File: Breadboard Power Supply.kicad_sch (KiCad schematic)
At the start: 15 parts, among them J1 Conn_01x02, J2 Conn_01x02, J3 Conn_01x03, J4 Screw_Terminal_01x02, J5 Barrel_Jack, U1 LM7805_TO220, U2 LM317_TO-220

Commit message: footprints
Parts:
- C1, C2, C3: footprint (none) -> Capacitor_THT:C_Disc_D3.0mm_W1.6mm_P2.50mm
- D1: footprint (none) -> LED_THT:LED_D5.0mm
- J1, J2: footprint (none) -> Connector_PinHeader_2.54mm:PinHeader_1x02_P2.54mm_Vertical
- J3: footprint (none) -> Connector_PinHeader_2.54mm:PinHeader_1x03_P2.54mm_Vertical
- J4: footprint (none) -> TerminalBlock:TerminalBlock_bornier-2_P5.08mm
- J5: footprint (none) -> Connector_BarrelJack:BarrelJack_SwitchcraftConxall_RAPC10U_Horizontal
- R1, R2, R3: footprint (none) -> PCM_Resistor_THT_AKL:R_Axial_DIN0204_L3.6mm_D1.6mm_P7.62mm_Horizontal
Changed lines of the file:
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@@
 			)
 		)
-		(property "Footprint" ""
+		(property "Footprint" "Capacitor_THT:C_Disc_D3.0mm_W1.6mm_P2.50mm"
 			(at 87.3252 66.04 0)
 			(effects
@@
 			)
 		)
-		(property "Footprint" ""
+		(property "Footprint" "PCM_Resistor_THT_AKL:R_Axial_DIN0204_L3.6mm_D1.6mm_P7.62mm_Horizontal"
 			(at 66.04 55.118 90)
 			(effects
@@
 			)
 		)
-		(property "Footprint" ""
+		(property "Footprint" "LED_THT:LED_D5.0mm"
 			(at 66.04 40.64 0)
 			(effects
@@
 			)
 		)
-		(property "Footprint" ""
+		(property "Footprint" "Capacitor_THT:C_Disc_D3.0mm_W1.6mm_P2.50mm"
 			(at 67.0052 66.04 0)
 			(effects
@@
 			)
 		)
-		(property "Footprint" ""
+		(property "Footprint" "Connector_PinHeader_2.54mm:PinHeader_1x02_P2.54mm_Vertical"
 			(at 66.04 72.39 0)
 			(effects
@@
 			)
 		)
-		(property "Footprint" ""
+		(property "Footprint" "TerminalBlock:TerminalBlock_bornier-2_P5.08mm"
 			(at 90.17 82.55 0)
 			(effects
@@
 			)
 		)
-		(property "Footprint" ""
+		(property "Footprint" "PCM_Resistor_THT_AKL:R_Axial_DIN0204_L3.6mm_D1.6mm_P7.62mm_Horizontal"
 			(at 86.36 55.118 90)
 			(effects
@@
 			)
 		)
-		(property "Footprint" ""
+		(property "Footprint" "PCM_Resistor_THT_AKL:R_Axial_DIN0204_L3.6mm_D1.6mm_P7.62mm_Horizontal"
 			(at 76.2 55.118 90)
 			(effects
@@
 			)
 		)
-		(property "Footprint" ""
+		(property "Footprint" "Connector_BarrelJack:BarrelJack_SwitchcraftConxall_RAPC10U_Horizontal"
 			(at 67.31 26.416 0)
 			(effects
@@
 			)
 		)
-		(property "Footprint" ""
+		(property "Footprint" "Connector_PinHeader_2.54mm:PinHeader_1x02_P2.54mm_Vertical"
 			(at 86.36 72.39 0)
 			(effects
@@
 			)
 		)
-		(property "Footprint" ""
+		(property "Footprint" "Connector_PinHeader_2.54mm:PinHeader_1x03_P2.54mm_Vertical"
 			(at 67.31 83.82 0)
 			(effects
@@
 			)
 		)
-		(property "Footprint" ""
+		(property "Footprint" "Capacitor_THT:C_Disc_D3.0mm_W1.6mm_P2.50mm"
 			(at 77.1652 66.04 0)
 			(effects

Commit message: schematic + placing
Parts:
- removed J5: Barrel_Jack, Connector_BarrelJack:BarrelJack_SwitchcraftConxall_RAPC10U_Horizontal, symbol Connector:Barrel_Jack
- added J5: Barrel_Jack_Switch, Connector_BarrelJack:BarrelJack_Horizontal, symbol Connector:Barrel_Jack_Switch
- added J6: Conn_01x03, Connector_PinHeader_2.54mm:PinHeader_1x03_P2.54mm_Vertical, symbol Connector_Generic:Conn_01x03
- added J7: Screw_Terminal_01x02, TerminalBlock:TerminalBlock_bornier-2_P5.08mm, symbol Connector:Screw_Terminal_01x02
- D1: footprint LED_THT:LED_D5.0mm -> (none)
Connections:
- net 12V: now reaches S1.1
- net 12V: now also C1.1, R1.2, U1.1 (VI), U2.3 (VI)
- net PWR_input: now reaches S1.2
- net PWR_input: now also J5.1
- net 5V: now reaches C3.1
- net 5V: now also J3.1 (Pin_1), U1.3 (VO), J6.1 (Pin_1)
- net GND: now reaches C3.2
- net GND: now also C1.2, C2.2, D1.1 (K), J1.2 (Pin_2), J2.2 (Pin_2), J4.2 (Pin_2), R3.1, U1.2 (GND), J5.2, J5.3, J7.2 (Pin_2)
- net at R1.1: now also D1.2 (A)
- net PWR_output: now reaches J1.1 (Pin_1)
- net PWR_output: now also J2.1 (Pin_1), J3.2 (Pin_2), J4.1 (Pin_1), J6.2 (Pin_2), J7.1 (Pin_1)
- net at U2.1 (ADJ): now also R2.1, R3.2
- net 3.3V: now reaches U2.2 (VO)
- net 3.3V: now also C2.1, J3.3 (Pin_3), R2.2, J6.3 (Pin_3)
- no-connect marks 0 -> 1
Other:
- moved on the sheet: C1, C2, C3, J1, J3, J4, R1, R2, R3, S1, U1, U2

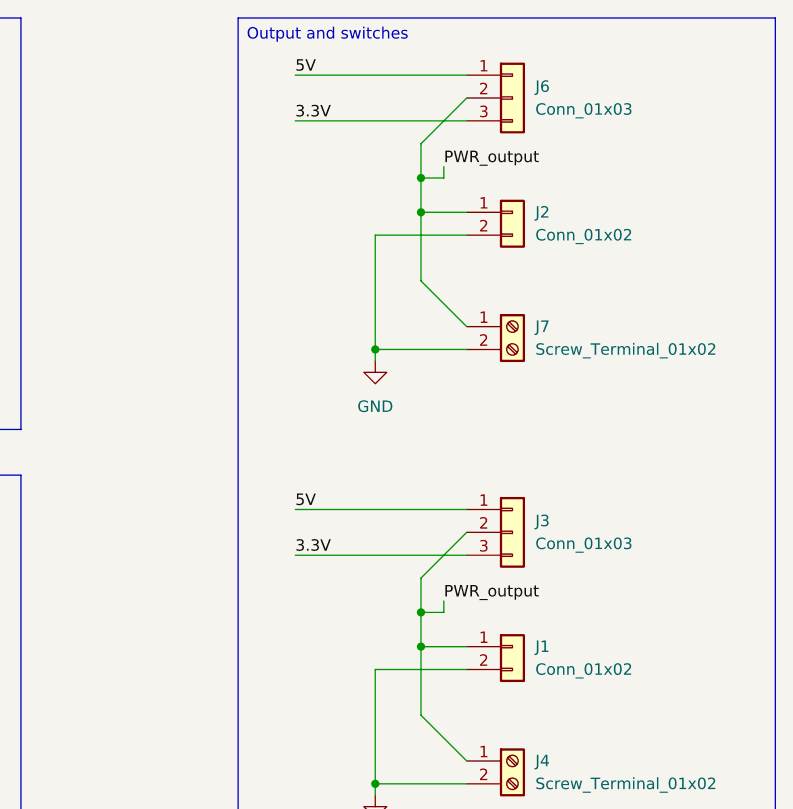
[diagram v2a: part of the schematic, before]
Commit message: fix short circuit pwr_output
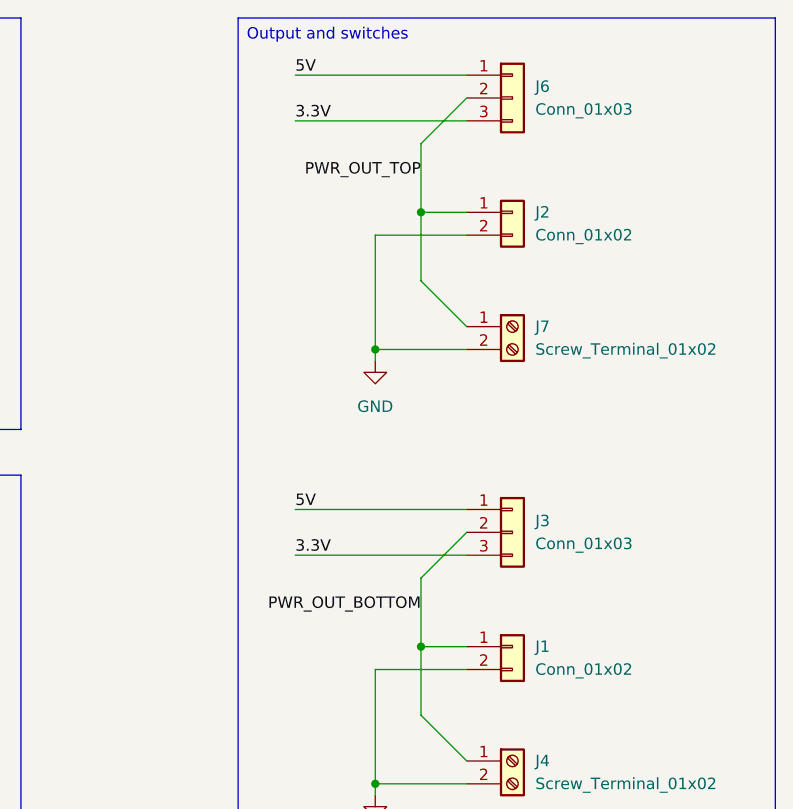
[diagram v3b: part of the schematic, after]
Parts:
- D1: footprint (none) -> PCM_LED_THT_AKL:LED_D5.0mm
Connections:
- net PWR_output renamed PWR_OUT_BOTTOM
- net PWR_OUT_BOTTOM: no longer J2.1 (Pin_1), J6.2 (Pin_2), J7.1 (Pin_1)
- new net PWR_OUT_TOP: J2.1 (Pin_1), J6.2 (Pin_2), J7.1 (Pin_1)
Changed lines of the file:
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@@
-	)
-	(junction
-		(at 209.55 63.5)
-		(diameter 0)
-		(color 0 0 0 0)
 	)
 	(junction
@@
 	(junction
 		(at 101.6 78.74)
-		(diameter 0)
-		(color 0 0 0 0)
-	)
-	(junction
-		(at 209.55 111.76)
 		(diameter 0)
 		(color 0 0 0 0)
@@
 	(wire
 		(pts
-			(xy 209.55 111.76) (xy 209.55 107.95)
-		)
-		(stroke
-			(width 0)
-			(type default)
-		)
-	)
-	(wire
-		(pts
 			(xy 204.47 118.11) (xy 214.63 118.11)
 		)
@@
 	(wire
 		(pts
-			(xy 209.55 63.5) (xy 209.55 59.69)
-		)
-		(stroke
-			(width 0)
-			(type default)
-		)
-	)
-	(wire
-		(pts
 			(xy 78.74 73.66) (xy 81.28 73.66)
 		)
@@
 	(wire
 		(pts
-			(xy 209.55 115.57) (xy 209.55 111.76)
+			(xy 209.55 107.95) (xy 209.55 115.57)
 		)
 		(stroke
@@
 	(wire
 		(pts
-			(xy 212.09 62.23) (xy 212.09 63.5)
-		)
-		(stroke
-			(width 0)
-			(type default)
-		)
-	)
-	(wire
-		(pts
 			(xy 114.3 107.95) (xy 114.3 106.68)
 		)
@@
 	(wire
 		(pts
-			(xy 212.09 111.76) (xy 209.55 111.76)
-		)
-		(stroke
-			(width 0)
-			(type default)
-		)
-	)
-	(wire
-		(pts
-			(xy 212.09 63.5) (xy 209.55 63.5)
-		)
-		(stroke
-			(width 0)
-			(type default)
-		)
-	)
-	(wire
-		(pts
 			(xy 116.84 78.74) (xy 116.84 73.66)
 		)
@@
 	(wire
 		(pts
-			(xy 209.55 67.31) (xy 209.55 63.5)
+			(xy 209.55 59.69) (xy 209.55 67.31)
 		)
 		(stroke
@@
 		(pts
 			(xy 127 106.68) (xy 144.78 106.68)
-		)
-		(stroke
-			(width 0)
-			(type default)
-		)
-	)
-	(wire
-		(pts
-			(xy 212.09 110.49) (xy 212.09 111.76)
 		)
 		(stroke
@@
 		)
 	)
-	(label "PWR_output"
-		(at 212.09 110.49 0)
+	(label "PWR_OUT_TOP"
+		(at 209.55 63.5 180)
 		(fields_autoplaced yes)
 		(effects
@@
 				(size 1.27 1.27)
 			)
-			(justify left bottom)
+			(justify right bottom)
 		)
 		(property "Netclass" "power_output"
-			(at 212.09 111.76 0)
+			(at 209.55 64.77 0)
 			(effects
 				(font
@@
 					(italic yes)
 				)
-				(justify left)
+				(justify right)
 			)
 		)
@@
 		)
 	)
-	(label "PWR_output"
-		(at 212.09 62.23 0)
+	(label "PWR_OUT_BOTTOM"
+		(at 209.55 111.76 180)
 		(fields_autoplaced yes)
 		(effects
@@
 				(size 1.27 1.27)
 			)
-			(justify left bottom)
+			(justify right bottom)
 		)
 		(property "Netclass" "power_output"
-			(at 212.09 63.5 0)
+			(at 209.55 113.03 0)
 			(effects
 				(font
@@
 					(italic yes)
 				)
-				(justify left)
+				(justify right)
 			)
 		)
@@
 			)
 		)
-		(property "Footprint" ""
+		(property "Footprint" "PCM_LED_THT_AKL:LED_D5.0mm"
 			(at 82.55 130.81 0)
 			(effects
